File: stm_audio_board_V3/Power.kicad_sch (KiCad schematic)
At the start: 94 parts, among them J5 Barrel_Jack_MountingPin, U1 IS42S16100H-7TL, U2 OP275, U3 7909, U4 OP275, U5 MIC2920A-3.3WS-TR, U6 7809, U9 MIC2920A-3.3WS-TR

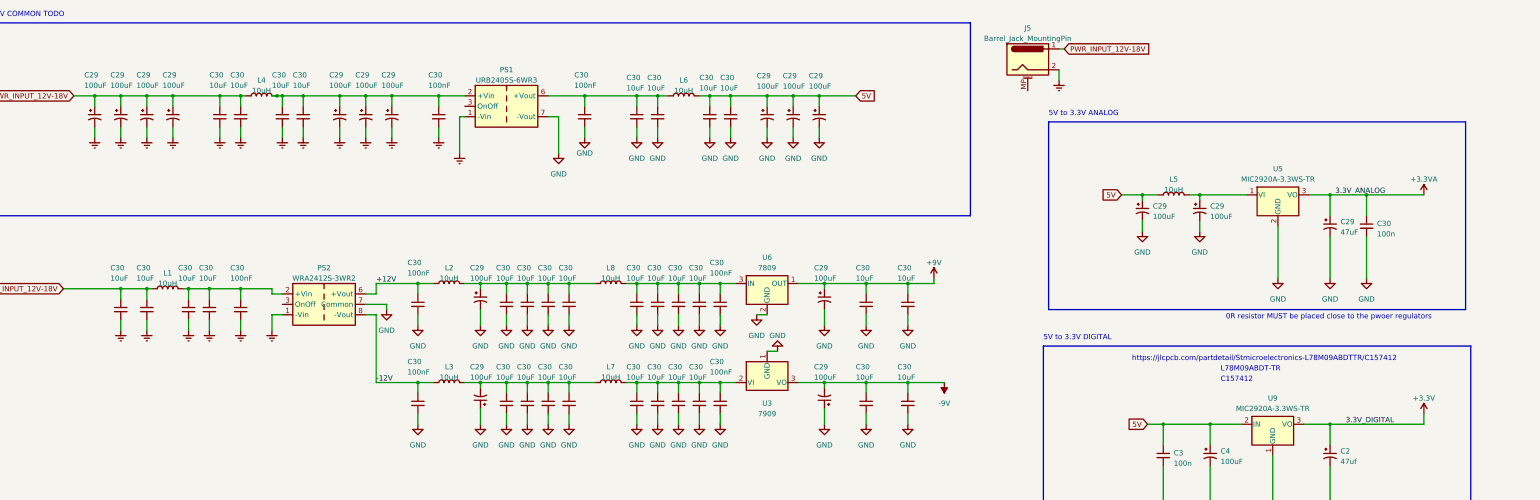
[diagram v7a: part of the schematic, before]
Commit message: Testpoints and parts for usb hub added
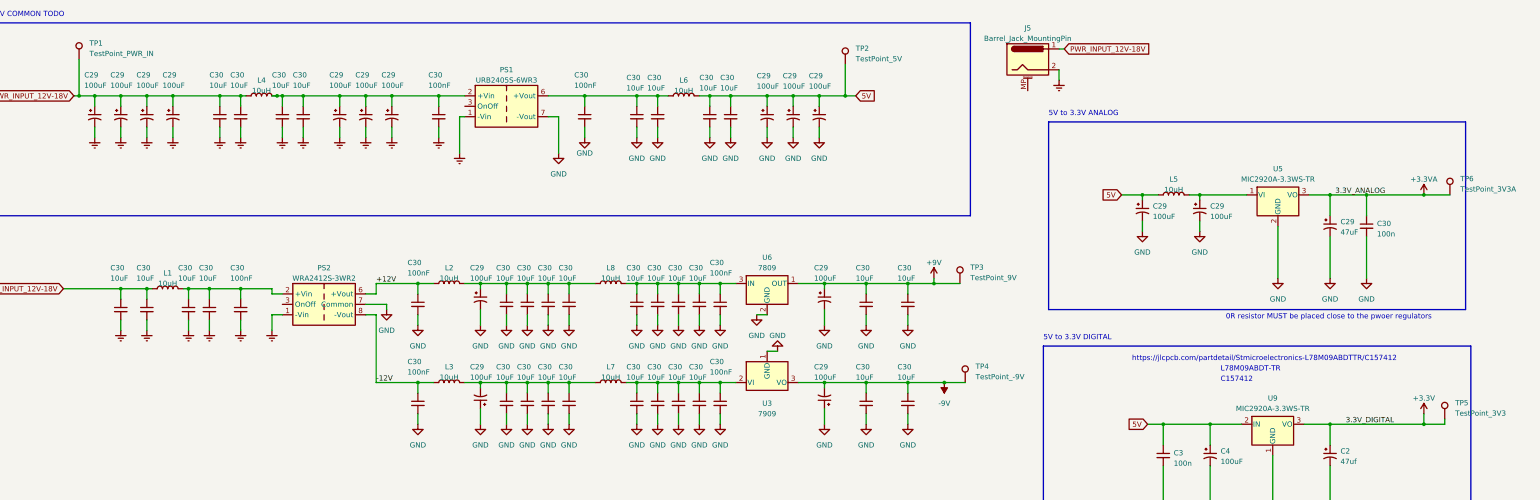
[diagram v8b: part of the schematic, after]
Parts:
- added TP1: TestPoint_PWR_IN, TestPoint:TestPoint_Pad_D1.5mm, symbol Connector:TestPoint
- added TP2: TestPoint_5V, TestPoint:TestPoint_Pad_D1.5mm, symbol Connector:TestPoint
- added TP3: TestPoint_9V, TestPoint:TestPoint_Pad_D1.5mm, symbol Connector:TestPoint
- added TP4: TestPoint_-9V, TestPoint:TestPoint_Pad_D1.5mm, symbol Connector:TestPoint
- added TP5: TestPoint_3V3, TestPoint:TestPoint_Pad_D1.5mm, symbol Connector:TestPoint
- added TP6: TestPoint_3V3A, TestPoint:TestPoint_Pad_D1.5mm, symbol Connector:TestPoint
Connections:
- net +3.3V: now also TP5.1
- net +3.3VA: now also TP6.1
- net +9V: now also TP3.1
- net -9V: now also TP4.1
- net 5V: now also TP2.1
- net PWR_INPUT_12V-18V: now also TP1.1
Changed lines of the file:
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@@
   (junction (at 72.39 85.09) (diameter 0) (color 0 0 0 0)
   )
+  (junction (at 254 83.82) (diameter 0) (color 0 0 0 0)
+  )
   (junction (at 160.02 107.95) (diameter 0) (color 0 0 0 0)
   )
@@
   (junction (at 133.35 219.71) (diameter 0) (color 0 0 0 0)
   )
+  (junction (at 45.72 38.1) (diameter 0) (color 0 0 0 0)
+  )
   (junction (at 283.21 220.98) (diameter 0) (color 0 0 0 0)
   )
@@
   (junction (at 149.86 83.82) (diameter 0) (color 0 0 0 0)
   )
+  (junction (at 373.38 62.23) (diameter 0) (color 0 0 0 0)
+  )
   (junction (at 90.17 251.46) (diameter 0) (color 0 0 0 0)
   )
@@
   (junction (at 303.53 218.44) (diameter 0) (color 0 0 0 0)
   )
+  (junction (at 232.41 38.1) (diameter 0) (color 0 0 0 0)
+  )
+  (junction (at 373.38 118.11) (diameter 0) (color 0 0 0 0)
+  )
   (junction (at 110.49 251.46) (diameter 0) (color 0 0 0 0)
   )
@@
   (junction (at 199.39 38.1) (diameter 0) (color 0 0 0 0)
   )
+  (junction (at 256.54 107.95) (diameter 0) (color 0 0 0 0)
+  )
   (junction (at 283.21 223.52) (diameter 0) (color 0 0 0 0)
   )
@@
     (stroke (width 0) (type default))
   )
+  (wire (pts (xy 378.46 118.11) (xy 378.46 116.84))
+    (stroke (width 0) (type default))
+  )
   (wire (pts (xy 201.93 115.57) (xy 201.93 118.11))
     (stroke (width 0) (type default))
@@
     (stroke (width 0) (type default))
   )
-  (wire (pts (xy 226.06 38.1) (xy 234.95 38.1))
+  (wire (pts (xy 226.06 38.1) (xy 232.41 38.1))
     (stroke (width 0) (type default))
   )
@@
     (stroke (width 0) (type default))
   )
+  (wire (pts (xy 260.35 83.82) (xy 254 83.82))
+    (stroke (width 0) (type default))
+  )
   (wire (pts (xy 350.52 62.23) (xy 359.41 62.23))
     (stroke (width 0) (type default))
@@
     (stroke (width 0) (type default))
   )
+  (wire (pts (xy 45.72 38.1) (xy 49.53 38.1))
+    (stroke (width 0) (type default))
+  )
   (wire (pts (xy 303.53 215.9) (xy 303.53 218.44))
     (stroke (width 0) (type default))
@@
     (stroke (width 0) (type default))
   )
-  (wire (pts (xy 373.38 115.57) (xy 373.38 118.11))
-    (stroke (width 0) (type default))
-  )
   (wire (pts (xy 90.17 251.46) (xy 99.06 251.46))
     (stroke (width 0) (type default))
@@
     (stroke (width 0) (type default))
   )
-  (wire (pts (xy 44.45 38.1) (xy 49.53 38.1))
+  (wire (pts (xy 44.45 38.1) (xy 45.72 38.1))
+    (stroke (width 0) (type default))
+  )
+  (wire (pts (xy 256.54 107.95) (xy 261.62 107.95))
     (stroke (width 0) (type default))
   )
@@
     (stroke (width 0) (type default))
   )
+  (wire (pts (xy 45.72 29.21) (xy 45.72 38.1))
+    (stroke (width 0) (type default))
+  )
   (wire (pts (xy 203.2 233.68) (xy 203.2 236.22))
     (stroke (width 0) (type default))
@@
     (stroke (width 0) (type default))
   )
+  (wire (pts (xy 373.38 115.57) (xy 373.38 118.11))
+    (stroke (width 0) (type default))
+  )
   (wire (pts (xy 154.94 107.95) (xy 160.02 107.95))
     (stroke (width 0) (type default))
@@
     (stroke (width 0) (type default))
   )
+  (wire (pts (xy 378.46 118.11) (xy 373.38 118.11))
+    (stroke (width 0) (type default))
+  )
   (wire (pts (xy 154.94 83.82) (xy 154.94 86.36))
     (stroke (width 0) (type default))
@@
     (stroke (width 0) (type default))
   )
+  (wire (pts (xy 232.41 38.1) (xy 234.95 38.1))
+    (stroke (width 0) (type default))
+  )
   (wire (pts (xy 179.07 83.82) (xy 181.61 83.82))
     (stroke (width 0) (type default))
@@
     (stroke (width 0) (type default))
   )
+  (wire (pts (xy 373.38 62.23) (xy 379.73 62.23))
+    (stroke (width 0) (type default))
+  )
   (wire (pts (xy 109.22 38.1) (xy 115.57 38.1))
     (stroke (width 0) (type default))
@@
     (stroke (width 0) (type default))
   )
+  (wire (pts (xy 232.41 30.48) (xy 232.41 38.1))
+    (stroke (width 0) (type default))
+  )
   (wire (pts (xy 55.88 38.1) (xy 55.88 40.64))
     (stroke (width 0) (type default))
@@
     )
   )
+  (symbol (lib_id "Connector:TestPoint") (at 232.41 30.48 0) (unit 1)
+    (in_bom yes) (on_board yes) (dnp no) (fields_autoplaced)
+    (property "Reference" "TP2" (at 234.95 26.543 0)
+      (effects (font (size 1.27 1.27)) (justify left))
+    )
+    (property "Value" "TestPoint_5V" (at 234.95 29.083 0)
+      (effects (font (size 1.27 1.27)) (justify left))
+    )
+    (property "Footprint" "TestPoint:TestPoint_Pad_D1.5mm" (at 237.49 30.48 0)
+      (effects (font (size 1.27 1.27)) hide)
+    )
+    (property "Datasheet" "~" (at 237.49 30.48 0)
+      (effects (font (size 1.27 1.27)) hide)
+    )
+    (pin "1")
+    (instances
+      (project "stm_audio_board_V3"
+        (path "/6997cf63-2615-4e49-9471-e7da1b6bae71/2eb2ee8f-ab98-4666-97f0-bfacb073bc88"
+          (reference "TP2") (unit 1)
+        )
+      )
+    )
+  )
   (symbol (lib_id "power:GND") (at 196.85 118.11 0) (unit 1)
     (in_bom yes) (on_board yes) (dnp no) (fields_autoplaced)
@@
     )
   )
+  (symbol (lib_id "Connector:TestPoint") (at 379.73 62.23 0) (unit 1)
+    (in_bom yes) (on_board yes) (dnp no) (fields_autoplaced)
+    (property "Reference" "TP6" (at 382.27 58.293 0)
+      (effects (font (size 1.27 1.27)) (justify left))
+    )
+    (property "Value" "TestPoint_3V3A" (at 382.27 60.833 0)
+      (effects (font (size 1.27 1.27)) (justify left))
+    )
+    (property "Footprint" "TestPoint:TestPoint_Pad_D1.5mm" (at 384.81 62.23 0)
+      (effects (font (size 1.27 1.27)) hide)
+    )
+    (property "Datasheet" "~" (at 384.81 62.23 0)
+      (effects (font (size 1.27 1.27)) hide)
+    )
+    (pin "1")
+    (instances
+      (project "stm_audio_board_V3"
+        (path "/6997cf63-2615-4e49-9471-e7da1b6bae71/2eb2ee8f-ab98-4666-97f0-bfacb073bc88"
+          (reference "TP6") (unit 1)
+        )
+      )
+    )
+  )
   (symbol (lib_id "Device:C_Small") (at 191.77 113.03 0) (unit 1)
     (in_bom yes) (on_board yes) (dnp no)
@@
     )
   )
+  (symbol (lib_id "Connector:TestPoint") (at 260.35 83.82 0) (unit 1)
+    (in_bom yes) (on_board yes) (dnp no) (fields_autoplaced)
+    (property "Reference" "TP3" (at 262.89 79.883 0)
+      (effects (font (size 1.27 1.27)) (justify left))
+    )
+    (property "Value" "TestPoint_9V" (at 262.89 82.423 0)
+      (effects (font (size 1.27 1.27)) (justify left))
+    )
+    (property "Footprint" "TestPoint:TestPoint_Pad_D1.5mm" (at 265.43 83.82 0)
+      (effects (font (size 1.27 1.27)) hide)
+    )
+    (property "Datasheet" "~" (at 265.43 83.82 0)
+      (effects (font (size 1.27 1.27)) hide)
+    )
+    (pin "1")
+    (instances
+      (project "stm_audio_board_V3"
+        (path "/6997cf63-2615-4e49-9471-e7da1b6bae71/2eb2ee8f-ab98-4666-97f0-bfacb073bc88"
+          (reference "TP3") (unit 1)
+        )
+      )
+    )
+  )
   (symbol (lib_id "Device:C_Small") (at 165.1 88.9 0) (unit 1)
     (in_bom yes) (on_board yes) (dnp no)
@@
     )
   )
+  (symbol (lib_id "Connector:TestPoint") (at 261.62 107.95 0) (unit 1)
+    (in_bom yes) (on_board yes) (dnp no) (fields_autoplaced)
+    (property "Reference" "TP4" (at 264.16 104.013 0)
+      (effects (font (size 1.27 1.27)) (justify left))
+    )
+    (property "Value" "TestPoint_-9V" (at 264.16 106.553 0)
+      (effects (font (size 1.27 1.27)) (justify left))
+    )
+    (property "Footprint" "TestPoint:TestPoint_Pad_D1.5mm" (at 266.7 107.95 0)
+      (effects (font (size 1.27 1.27)) hide)
+    )
+    (property "Datasheet" "~" (at 266.7 107.95 0)
+      (effects (font (size 1.27 1.27)) hide)
+    )
+    (pin "1")
+    (instances
+      (project "stm_audio_board_V3"
+        (path "/6997cf63-2615-4e49-9471-e7da1b6bae71/2eb2ee8f-ab98-4666-97f0-bfacb073bc88"
+          (reference "TP4") (unit 1)
+        )
+      )
+    )
+  )
   (symbol (lib_id "Device:C_Small") (at 181.61 43.18 0) (unit 1)
     (in_bom yes) (on_board yes) (dnp no)
@@
     )
   )
+  (symbol (lib_id "Connector:TestPoint") (at 45.72 29.21 0) (unit 1)
+    (in_bom yes) (on_board yes) (dnp no) (fields_autoplaced)
+    (property "Reference" "TP1" (at 48.26 25.273 0)
+      (effects (font (size 1.27 1.27)) (justify left))
+    )
+    (property "Value" "TestPoint_PWR_IN" (at 48.26 27.813 0)
+      (effects (font (size 1.27 1.27)) (justify left))
+    )
+    (property "Footprint" "TestPoint:TestPoint_Pad_D1.5mm" (at 50.8 29.21 0)
+      (effects (font (size 1.27 1.27)) hide)
+    )
+    (property "Datasheet" "~" (at 50.8 29.21 0)
+      (effects (font (size 1.27 1.27)) hide)
+    )
+    (pin "1")
+    (instances
+      (project "stm_audio_board_V3"
+        (path "/6997cf63-2615-4e49-9471-e7da1b6bae71/2eb2ee8f-ab98-4666-97f0-bfacb073bc88"
+          (reference "TP1") (unit 1)
+        )
+      )
+    )
+  )
   (symbol (lib_id "power:GND") (at 318.77 71.12 0) (unit 1)
     (in_bom yes) (on_board yes) (dnp no) (fields_autoplaced)
@@
         )
       )
+    )
+  )
+  (symbol (lib_id "Connector:TestPoint") (at 378.46 116.84 0) (unit 1)
+    (in_bom yes) (on_board yes) (dnp no) (fields_autoplaced)
+    (property "Reference" "TP5" (at 381 112.903 0)
+      (effects (font (size 1.27 1.27)) (justify left))
+    )
+    (property "Value" "TestPoint_3V3" (at 381 115.443 0)
+      (effects (font (size 1.27 1.27)) (justify left))
+    )
+    (property "Footprint" "TestPoint:TestPoint_Pad_D1.5mm" (at 383.54 116.84 0)
+      (effects (font (size 1.27 1.27)) hide)
+    )
+    (property "Datasheet" "~" (at 383.54 116.84 0)
+      (effects (font (size 1.27 1.27)) hide)
+    )
+    (pin "1")
+    (instances
+      (project "stm_audio_board_V3"
+        (path "/6997cf63-2615-4e49-9471-e7da1b6bae71/2eb2ee8f-ab98-4666-97f0-bfacb073bc88"
+          (reference "TP5") (unit 1)
+        )
+      )
